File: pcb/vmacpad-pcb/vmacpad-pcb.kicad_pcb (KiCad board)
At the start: 2 copper layers, 134.7 x 126.1 mm, 79 parts, among them J1 TYPE-C-31-M12_13, J2 Conn_01x04_Pin, J3 Conn_01x04_Pin, K1 1u, K10 1u, K12 2.25u, K13 1u, K14 1u, K16 1u, K17 1u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

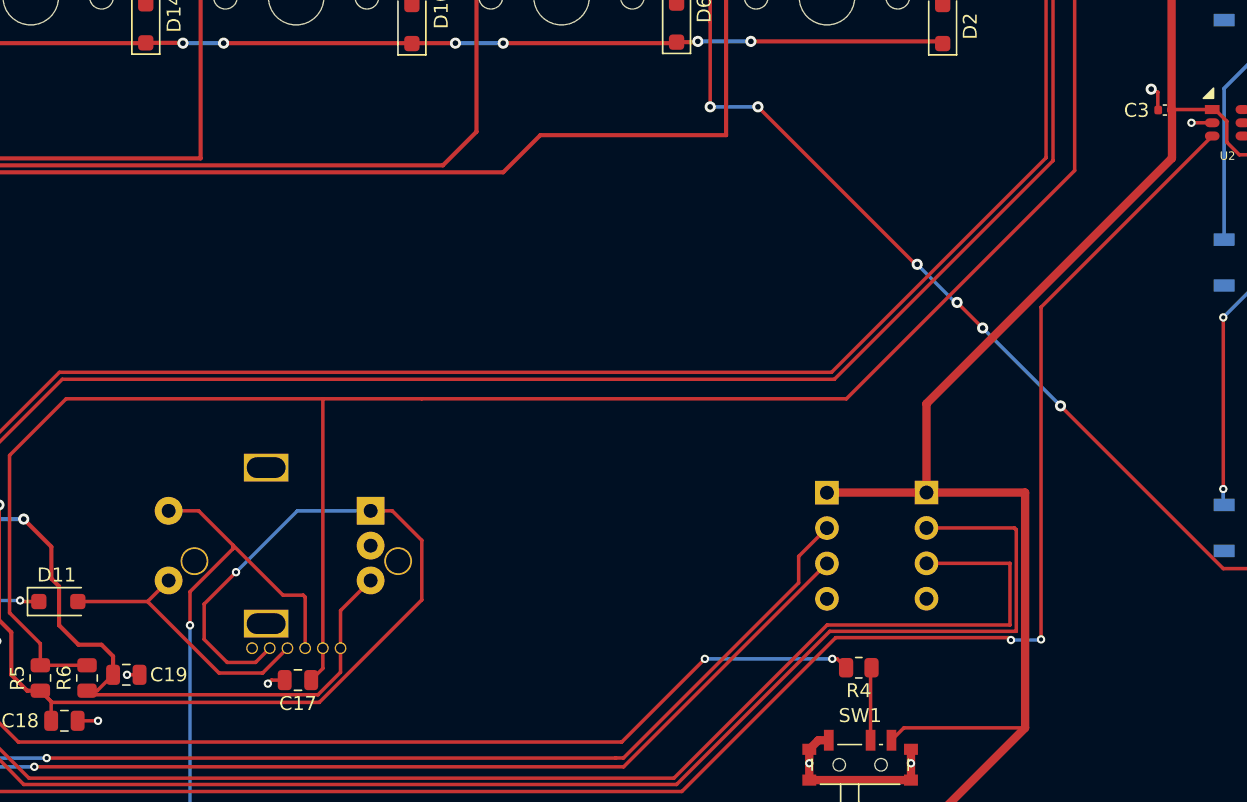
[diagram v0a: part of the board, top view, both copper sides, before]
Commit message: Fix minor placements
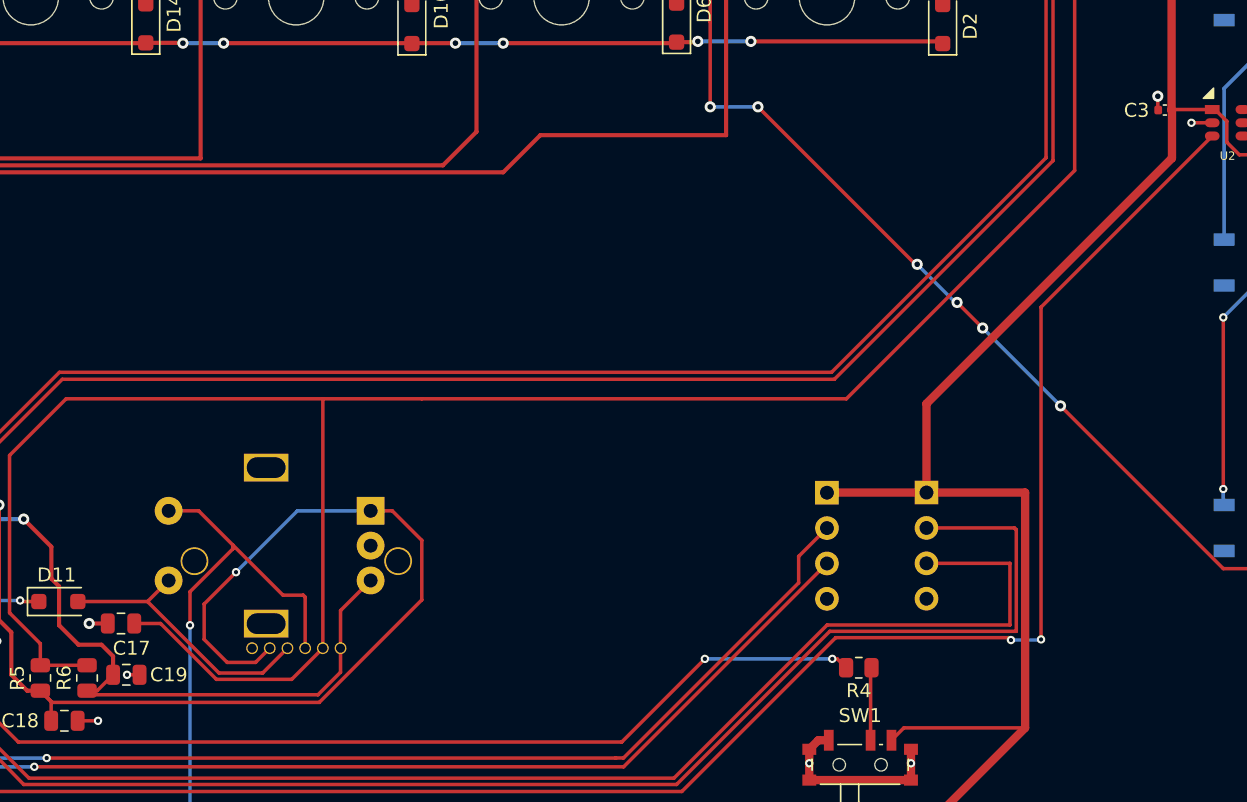
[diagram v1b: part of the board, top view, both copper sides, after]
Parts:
- moved C17 13.3 mm to (130.3, 178.3)
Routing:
- net VCC: track 367.9 -> 381.4 mm
- net GND: track 65.2 -> 64.7 mm
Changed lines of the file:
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@@
   )
   (footprint "Capacitor_SMD:C_0805_2012Metric" (layer "F.Cu")
-    (at 143.002 182.372 180)
+    (at 130.302 178.308 180)
     (descr "Capacitor SMD 0805 (2012 Metric), square (rectangular) end terminal, IPC_7351 nominal, (Body size source: IPC-SM-782 page 76, https://www.pcb-3d.com/wordpress/wp-content/uploads/ipc-sm-782a_amendment_1_and_2.pdf, https://docs.google.com/spreadsheets/d/1BsfQQcO9C6DZCsRaXUlFlo91Tg2WpOkGARC1WS5S8t0/edit?usp=sharing), generated with kicad-footprint-generator")
     (tags "capacitor")
@@
     (property "ki_keywords" "cap capacitor")
     (attr smd)
-    (fp_text reference "C17" (at 0 -1.68) (layer "F.SilkS")
+    (fp_text reference "C17" (at -0.762 -1.778) (layer "F.SilkS")
         (effects (font (size 1 1) (thickness 0.15)))
     )
@@
   (segment (start 217.421 101.219) (end 219.202 99.438) (width 0.6) (layer "F.Cu") (net 1))
   (segment (start 214.032 103.389305) (end 211.861695 101.219) (width 0.6) (layer "F.Cu") (net 1))
-  (segment (start 143.952 182.372) (end 144.79 181.534) (width 0.254) (layer "F.Cu") (net 2))
   (segment (start 216.789 131.699) (end 218.097 133.007) (width 0.6) (layer "F.Cu") (net 2))
   (segment (start 122.301 177.546) (end 122.301 166.243) (width 0.254) (layer "F.Cu") (net 2))
@@
   (segment (start 222.25 126.238) (end 216.789 131.699) (width 0.6) (layer "F.Cu") (net 2))
   (segment (start 216.789 137.16) (end 218.097 137.16) (width 0.254) (layer "F.Cu") (net 2))
+  (segment (start 142.55325 182.318) (end 137.149547 182.318) (width 0.254) (layer "F.Cu") (net 2))
   (segment (start 144.78 162.179) (end 151.892 162.179) (width 0.254) (layer "F.Cu") (net 2))
   (segment (start 217.297 168.783) (end 216.408 169.672) (width 0.6) (layer "F.Cu") (net 2))
   (segment (start 220.853 118.921) (end 220.902 118.921) (width 0.6) (layer "F.Cu") (net 2))
+  (segment (start 133.139547 178.308) (end 131.252 178.308) (width 0.254) (layer "F.Cu") (net 2))
   (segment (start 144.79 162.189) (end 144.78 162.179) (width 0.254) (layer "F.Cu") (net 2))
   (segment (start 127.8636 181.3071) (end 124.5108 181.3071) (width 0.254) (layer "F.Cu") (net 2))
-  (segment (start 144.79 181.534) (end 144.79 180.08125) (width 0.254) (layer "F.Cu") (net 2))
   (segment (start 222.25 120.269) (end 222.25 126.238) (width 0.6) (layer "F.Cu") (net 2))
   (segment (start 198.755 126.492) (end 205.105 120.142) (width 0.254) (layer "F.Cu") (net 2))
@@
   (segment (start 124.5108 179.7558) (end 122.301 177.546) (width 0.254) (layer "F.Cu") (net 2))
   (segment (start 214.1645 141.4526) (end 214.1645 139.7845) (width 0.254) (layer "F.Cu") (net 2))
+  (segment (start 144.79 180.08125) (end 142.55325 182.318) (width 0.254) (layer "F.Cu") (net 2))
+  (segment (start 137.149547 182.318) (end 133.139547 178.308) (width 0.254) (layer "F.Cu") (net 2))
   (segment (start 205.105 120.142) (end 212.979 120.142) (width 0.254) (layer "F.Cu") (net 2))
   (segment (start 222.885 102.236) (end 222.883 102.238) (width 0.6) (layer "F.Cu") (net 2))
@@
   (segment (start 208.6297 142.367) (end 207.137 142.367) (width 0.254) (layer "F.Cu") (net 3))
   (segment (start 102.41395 189.86875) (end 102.2096 189.6644) (width 0.254) (layer "F.Cu") (net 3))
+  (segment (start 129.352 178.308) (end 128.016 178.308) (width 0.3) (layer "F.Cu") (net 3))
   (segment (start 216.50355 141.4526) (end 216.52895 141.478) (width 0.254) (layer "F.Cu") (net 3))
   (segment (start 180.35625 186.68875) (end 179.70625 187.33875) (width 0.6) (layer "F.Cu") (net 3))
@@
   (segment (start 205.5622 126.2144) (end 207.2404 126.2144) (width 0.6) (layer "F.Cu") (net 3))
   (segment (start 103.8625 189.86875) (end 102.41395 189.86875) (width 0.254) (layer "F.Cu") (net 3))
-  (segment (start 141.097 182.372) (end 140.843 182.626) (width 0.254) (layer "F.Cu") (net 3))
   (segment (start 100.0024 189.6644) (end 99.949 189.611) (width 0.254) (layer "F.Cu") (net 3))
   (segment (start 106.2875 181.0093) (end 106.2875 182.44375) (width 0.254) (layer "F.Cu") (net 3))
@@
   (segment (start 218.2368 112.7252) (end 214.4395 116.5225) (width 0.6) (layer "F.Cu") (net 3))
   (segment (start 97.721 185.44) (end 97.721 185.194) (width 0.254) (layer "F.Cu") (net 3))
-  (segment (start 142.052 182.372) (end 141.097 182.372) (width 0.254) (layer "F.Cu") (net 3))
   (segment (start 105.725764 195.199) (end 105.173562 195.199) (width 0.254) (layer "F.Cu") (net 3))
   (segment (start 127.188 185.293) (end 128.651 185.293) (width 0.254) (layer "F.Cu") (net 3))
@@
   (segment (start 113.256 196.204562) (end 113.256 196.215) (width 0.254) (layer "F.Cu") (net 3))
   (segment (start 112.7875 195.736062) (end 113.256 196.204562) (width 0.254) (layer "F.Cu") (net 3))
-  (segment (start 204.2497 139.954) (end 204.724 140.1743) (width 0.254) (layer "F.Cu") (net 3))
   (segment (start 179.70625 189.54875) (end 187.00625 189.54875) (width 0.6) (layer "F.Cu") (net 3))
   (segment (start 213.233 125.476) (end 213.233 126.492) (width 0.6) (layer "F.Cu") (net 3))
@@
   (via (at 218.821 125.349) (size 0.8) (drill 0.4) (layers "F.Cu" "B.Cu") (net 3))
   (via (at 110.363 195.33) (size 0.6) (drill 0.3) (layers "F.Cu" "B.Cu") (net 3))
+  (via (at 128.016 178.308) (size 0.8) (drill 0.4) (layers "F.Cu" "B.Cu") (net 3))
   (via (at 98.806 182.372) (size 0.6) (drill 0.3) (layers "F.Cu" "B.Cu") (free) (net 3))
-  (via (at 140.843 182.626) (size 0.6) (drill 0.3) (layers "F.Cu" "B.Cu") (net 3))
   (via (at 94.488 184.658) (size 0.6) (drill 0.3) (layers "F.Cu" "B.Cu") (free) (net 3))
   (via (at 207.264 126.238) (size 0.8) (drill 0.4) (layers "F.Cu" "B.Cu") (net 3))
@@
   (via (at 218.2368 112.7252) (size 0.8) (drill 0.4) (layers "F.Cu" "B.Cu") (net 3))
   (via (at 94.361 188.087) (size 0.6) (drill 0.3) (layers "F.Cu" "B.Cu") (free) (net 3))
-  (via (at 204.2497 139.954) (size 0.8) (drill 0.4) (layers "F.Cu" "B.Cu") (net 3))
+  (via (at 204.724 140.462) (size 0.8) (drill 0.4) (layers "F.Cu" "B.Cu") (net 3))
   (via (at 100.457 183.388) (size 0.6) (drill 0.3) (layers "F.Cu" "B.Cu") (net 3))
   (via (at 187.00625 188.341) (size 0.6) (drill 0.3) (layers "F.Cu" "B.Cu") (net 3))

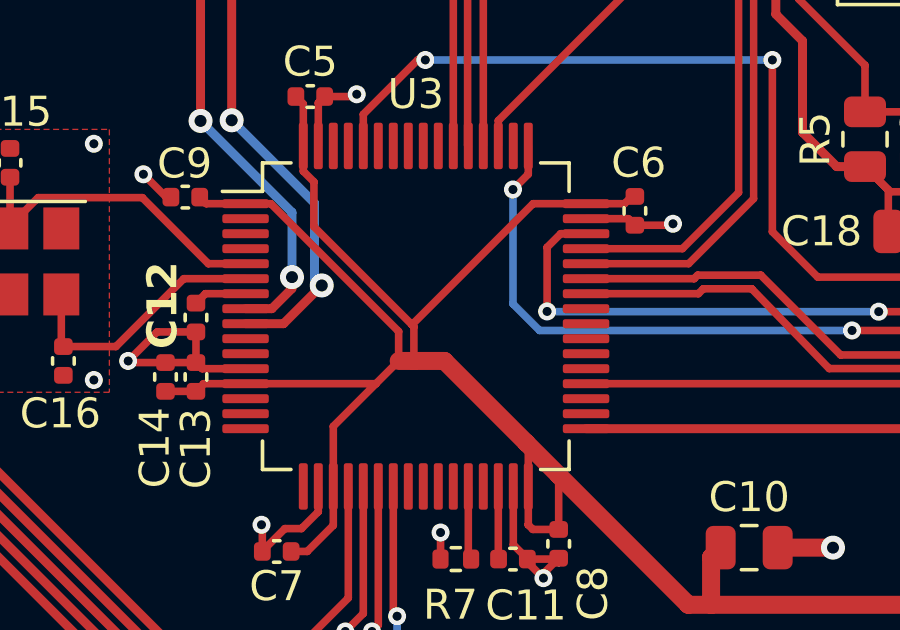
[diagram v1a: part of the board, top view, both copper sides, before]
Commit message: Fix power tracks
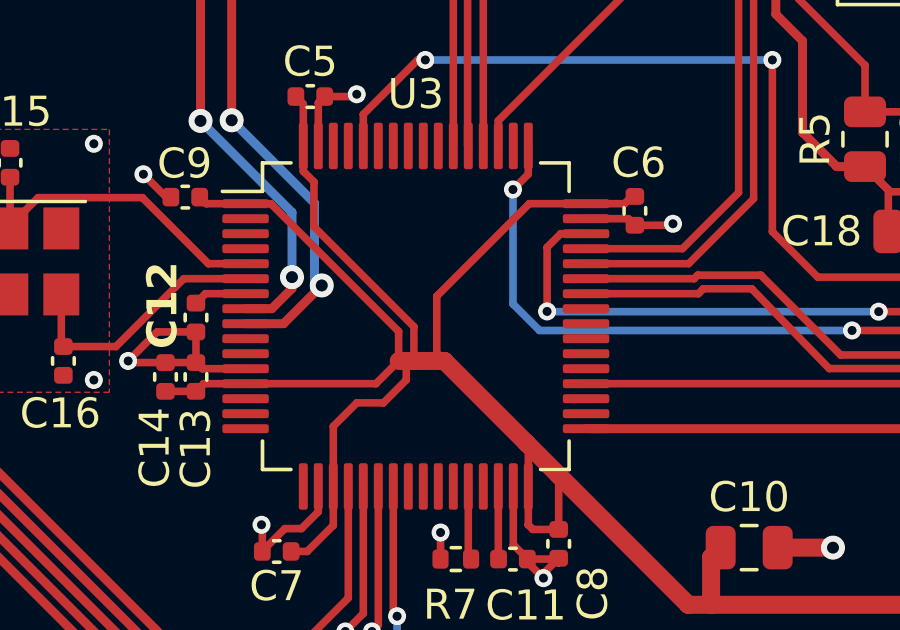
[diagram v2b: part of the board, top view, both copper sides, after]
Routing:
- net +3.3V: track 255.0 -> 257.7 mm
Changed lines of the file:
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@@
   (segment (start 113.2875 193.79375) (end 113.2875 192.406212) (width 0.254) (layer "F.Cu") (net 9))
   (segment (start 114.3 193.421) (end 114.301144 193.419856) (width 0.254) (layer "F.Cu") (net 9))
+  (segment (start 103.8625 190.36875) (end 108.20825 190.36875) (width 0.254) (layer "F.Cu") (net 9))
   (segment (start 186.494 185.801) (end 195.199 185.801) (width 0.254) (layer "F.Cu") (net 9))
   (segment (start 105.7875 181.0451) (end 105.5396 180.7972) (width 0.254) (layer "F.Cu") (net 9))
   (segment (start 101.1936 190.6244) (end 102.2096 190.6244) (width 0.254) (layer "F.Cu") (net 9))
-  (segment (start 103.8625 190.36875) (end 108.20825 190.36875) (width 0.254) (layer "F.Cu") (net 9))
   (segment (start 119.38 196.154) (end 119.38 197.739) (width 0.6) (layer "F.Cu") (net 9))
   (segment (start 113.221644 192.340356) (end 110.492288 189.611) (width 0.6) (layer "F.Cu") (net 9))
+  (segment (start 106.7875 191.7895) (end 107.569 191.008) (width 0.254) (layer "F.Cu") (net 9))
+  (segment (start 108.458 191.008) (end 109.22 190.246) (width 0.254) (layer "F.Cu") (net 9))
   (segment (start 105.918 195.961) (end 105.382 195.961) (width 0.254) (layer "F.Cu") (net 9))
   (segment (start 215 144.664) (end 210.577 144.664) (width 0.254) (layer "F.Cu") (net 9))
   (segment (start 188.11875 162.52825) (end 205.74 144.907) (width 0.6) (layer "F.Cu") (net 9))
-  (segment (start 105.7875 182.44375) (end 105.7875 183.287264) (width 0.254) (layer "F.Cu") (net 9))
   (segment (start 119.7 195.834) (end 119.38 196.154) (width 0.6) (layer "F.Cu") (net 9))
   (segment (start 116.84 184.1272) (end 116.7358 184.1272) (width 0.254) (layer "F.Cu") (net 9))
+  (segment (start 106.142236 183.642) (end 106.142236 185.136236) (width 0.254) (layer "F.Cu") (net 9))
   (segment (start 102.55275 184.36875) (end 102.334 184.15) (width 0.254) (layer "F.Cu") (net 9))
   (segment (start 110.492288 189.611) (end 109.474 189.611) (width 0.6) (layer "F.Cu") (net 9))
-  (segment (start 108.20825 190.36875) (end 108.966 189.611) (width 0.254) (layer "F.Cu") (net 9))
-  (segment (start 106.7875 191.7895) (end 108.20825 190.36875) (width 0.254) (layer "F.Cu") (net 9))
-  (segment (start 109.474 188.468) (end 109.474 189.611) (width 0.254) (layer "F.Cu") (net 9))
-  (segment (start 106.142236 183.642) (end 106.142236 185.136236) (width 0.254) (layer "F.Cu") (net 9))
   (segment (start 113.2875 192.406212) (end 113.221644 192.340356) (width 0.254) (layer "F.Cu") (net 9))
   (segment (start 188.11875 168.91) (end 195.199 168.91) (width 0.6) (layer "F.Cu") (net 9))
@@
   (segment (start 195.199 185.801) (end 183.261 197.739) (width 0.6) (layer "F.Cu") (net 9))
   (segment (start 113.439 195.227) (end 113.284 195.072) (width 0.254) (layer "F.Cu") (net 9))
-  (segment (start 113.44625 184.36875) (end 109.4105 188.4045) (width 0.254) (layer "F.Cu") (net 9))
   (segment (start 102.46525 190.36875) (end 103.8625 190.36875) (width 0.254) (layer "F.Cu") (net 9))
-  (segment (start 109.474 189.611) (end 108.966 189.611) (width 0.6) (layer "F.Cu") (net 9))
   (segment (start 106.7875 193.79375) (end 106.7875 191.7895) (width 0.254) (layer "F.Cu") (net 9))
   (segment (start 195.199 168.91) (end 195.199 185.801) (width 0.6) (layer "F.Cu") (net 9))
@@
   (segment (start 103.8625 184.36875) (end 104.706014 184.36875) (width 0.254) (layer "F.Cu") (net 9))
   (segment (start 106.7875 193.79375) (end 106.7875 195.0915) (width 0.254) (layer "F.Cu") (net 9))
+  (segment (start 105.7875 183.287264) (end 106.142236 183.642) (width 0.254) (layer "F.Cu") (net 9))
   (segment (start 205.74 144.907) (end 205.74 141.4913) (width 0.6) (layer "F.Cu") (net 9))
+  (segment (start 108.20825 190.36875) (end 108.966 189.611) (width 0.254) (layer "F.Cu") (net 9))
   (segment (start 113.284 195.072) (end 113.2875 195.0685) (width 0.254) (layer "F.Cu") (net 9))
   (segment (start 185.60625 186.68875) (end 186.494 185.801) (width 0.254) (layer "F.Cu") (net 9))
   (segment (start 106.7875 195.0915) (end 105.918 195.961) (width 0.254) (layer "F.Cu") (net 9))
-  (segment (start 106.142236 185.136236) (end 109.4105 188.4045) (width 0.254) (layer "F.Cu") (net 9))
   (segment (start 208.8347 141.417) (end 208.6297 141.417) (width 0.254) (layer "F.Cu") (net 9))
   (segment (start 210.577 144.664) (end 209.677 143.764) (width 0.254) (layer "F.Cu") (net 9))
-  (segment (start 105.7875 183.287264) (end 106.142236 183.642) (width 0.254) (layer "F.Cu") (net 9))
+  (segment (start 107.569 191.008) (end 108.458 191.008) (width 0.254) (layer "F.Cu") (net 9))
+  (segment (start 109.474 189.611) (end 109.22 189.611) (width 0.6) (layer "F.Cu") (net 9))
   (segment (start 188.11875 168.91) (end 180.985 168.91) (width 0.6) (layer "F.Cu") (net 9))
+  (segment (start 109.22 190.246) (end 109.22 189.611) (width 0.254) (layer "F.Cu") (net 9))
   (segment (start 183.261 197.739) (end 119.38 197.739) (width 0.6) (layer "F.Cu") (net 9))
   (segment (start 108.966 188.628736) (end 108.966 189.611) (width 0.254) (layer "F.Cu") (net 9))
   (segment (start 116.7358 184.1272) (end 116.49425 184.36875) (width 0.254) (layer "F.Cu") (net 9))
+  (segment (start 115.2125 184.36875) (end 113.31925 184.36875) (width 0.254) (layer "F.Cu") (net 9))
+  (segment (start 110.236 187.452) (end 110.236 189.354712) (width 0.254) (layer "F.Cu") (net 9))
   (segment (start 180.985 168.91) (end 180.975 168.92) (width 0.6) (layer "F.Cu") (net 9))
+  (segment (start 109.22 189.611) (end 108.966 189.611) (width 0.6) (layer "F.Cu") (net 9))
   (segment (start 188.11875 168.91) (end 188.11875 162.52825) (width 0.6) (layer "F.Cu") (net 9))
+  (segment (start 110.236 189.354712) (end 110.492288 189.611) (width 0.254) (layer "F.Cu") (net 9))
   (segment (start 205.74 141.4913) (end 205.7013 141.4526) (width 0.6) (layer "F.Cu") (net 9))
   (segment (start 102.2096 190.6244) (end 102.46525 190.36875) (width 0.254) (layer "F.Cu") (net 9))
+  (segment (start 109.474 188.468) (end 109.474 189.611) (width 0.254) (layer "F.Cu") (net 9))
   (segment (start 114.3 195.227) (end 113.439 195.227) (width 0.254) (layer "F.Cu") (net 9))
-  (segment (start 109.4105 188.4045) (end 109.474 188.468) (width 0.254) (layer "F.Cu") (net 9))
+  (segment (start 105.7875 182.44375) (end 105.7875 183.287264) (width 0.254) (layer "F.Cu") (net 9))
+  (segment (start 106.142236 185.136236) (end 109.474 188.468) (width 0.254) (layer "F.Cu") (net 9))
+  (segment (start 113.31925 184.36875) (end 110.236 187.452) (width 0.254) (layer "F.Cu") (net 9))
   (segment (start 216.027 143.637) (end 215 144.664) (width 0.254) (layer "F.Cu") (net 9))
   (segment (start 205.712 130.838) (end 208.94 127.61) (width 0.6) (layer "F.Cu") (net 9))
@@
   (segment (start 103.8625 184.36875) (end 102.55275 184.36875) (width 0.254) (layer "F.Cu") (net 9))
   (segment (start 116.49425 184.36875) (end 115.2125 184.36875) (width 0.254) (layer "F.Cu") (net 9))
-  (segment (start 115.2125 184.36875) (end 113.44625 184.36875) (width 0.254) (layer "F.Cu") (net 9))
   (segment (start 113.2875 195.0685) (end 113.2875 193.79375) (width 0.254) (layer "F.Cu") (net 9))
   (segment (start 104.706014 184.36875) (end 108.966 188.628736) (width 0.254) (layer "F.Cu") (net 9))
